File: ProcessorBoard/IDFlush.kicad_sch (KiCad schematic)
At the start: 8 parts, among them U5 74AHCT245, U6 74AHCT16245, U7 74AHCT245, U8 74AHCT16245

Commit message: ProcessorBoard: Update with changes to Control module Ctl_Mid/Ctl_EX issue
This fixes the second issue in Rev D with Ctl_Mid/Ctl_EX.

Two more signals in Hazard Control were using signals from Ctl_Mid when
they should have instead been using signals from Ctl_EX. This fixes an
issue where the control module is unable to correctly detect a RAW hazard
in the EX stage.
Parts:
- U5, U7: value 74AHCT245 -> 74HC245
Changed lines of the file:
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@@
   (paper "A4")
   (title_block
-    (date "2023-11-15")
+    (date "2023-11-19")
     (rev "A")
     (comment 3 "registers must be all ones, which represents a NOP.")
@@
     )
   )
-  (symbol (lib_id "Device:C") (at 33.02 184.15 0) (unit 1)
+  (symbol (lib_id "Device:C") (at 33.02 184.15 0) (mirror y) (unit 1)
     (in_bom yes) (on_board yes) (dnp no)
-    (property "Reference" "C7" (at 35.941 182.9816 0)
+    (property "Reference" "C7" (at 30.099 182.9816 0)
       (effects (font (size 1.27 1.27)) (justify left))
     )
-    (property "Value" "0.1uF" (at 35.941 185.293 0)
+    (property "Value" "0.1uF" (at 30.099 185.293 0)
       (effects (font (size 1.27 1.27)) (justify left))
     )
-    (property "Footprint" "Capacitor_SMD:C_0603_1608Metric_Pad1.08x0.95mm_HandSolder" (at 33.9852 187.96 0)
+    (property "Footprint" "Capacitor_SMD:C_0603_1608Metric_Pad1.08x0.95mm_HandSolder" (at 32.0548 187.96 0)
       (effects (font (size 1.27 1.27)) hide)
     )
@@
       (effects (font (size 1.27 1.27)) (justify left))
     )
-    (property "Value" "74AHCT245" (at 96.8659 114.935 0)
+    (property "Value" "74HC245" (at 96.8659 114.935 0)
       (effects (font (size 1.27 1.27)) (justify left))
     )
@@
       (effects (font (size 1.27 1.27)) (justify left))
     )
-    (property "Value" "74AHCT245" (at 214.2841 114.935 0)
+    (property "Value" "74HC245" (at 214.2841 114.935 0)
       (effects (font (size 1.27 1.27)) (justify left))
     )

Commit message: ProcessorBoard: Use 74ABT where possible over 74AHCT
In several places, the schematics specify 74HC and 74AHCT versions of ICs
where choosing 74ABT would be fine, and would improve performance.
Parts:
- U5, U7: value 74HC245 -> 74ABT245; Mouser (none) -> https://www.mouser.com/ProductDetail/Texas-Instruments/SN74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
- U6, U8: value 74AHCT16245 -> 74ABT16245; Mouser https://www.mouser.com/ProductDetail/Texas-Instruments/74AH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 -> https://www.mouser.com/ProductDetail/Texas-Instruments/74AB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
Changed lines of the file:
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@@
       (effects (font (size 1.27 1.27)) (justify left))
     )
-    (property "Value" "74AHCT16245" (at 110.49 34.925 0)
+    (property "Value" "74ABT16245" (at 110.49 34.925 0)
       (effects (font (size 1.27 1.27)) (justify left))
     )
@@
       (effects (font (size 1.27 1.27)) hide)
     )
-    (property "Datasheet" "" (at 106.68 58.42 0)
-      (effects (font (size 1.27 1.27)) hide)
-    )
-    (property "Mouser" "https://www.mouser.com/ProductDetail/Texas-Instruments/74AHCT16245DLRG4?qs=%2Fha2pyFaduixTLlQ%252B3rIFW8KDPMe6E5CxoQ2Fc519Y9S5BWJ%252B%2FVWeIYQshP1VtN3&utm_source=octopart&utm_medium=aggregator&utm_campaign=595-74AHCT16245DLRG4&utm_content=Texas%20Instruments" (at 101.6 50.8 0)
+    (property "Datasheet" "https://www.ti.com/general/docs/suppproductinfo.tsp?distId=26&gotoUrl=https://www.ti.com/lit/gpn/sn74abt16245a" (at 106.68 58.42 0)
+      (effects (font (size 1.27 1.27)) hide)
+    )
+    (property "Mouser" "https://www.mouser.com/ProductDetail/Texas-Instruments/74ABT16245ADGGRG4?qs=AsTZqt%2FmeqlOzxDYtxnpKQ%3D%3D" (at 101.6 50.8 0)
       (effects (font (size 1.27 1.27)) hide)
     )
@@
       (effects (font (size 1.27 1.27)) (justify left))
     )
-    (property "Value" "74HC245" (at 96.8659 114.935 0)
+    (property "Value" "74ABT245" (at 96.8659 114.935 0)
       (effects (font (size 1.27 1.27)) (justify left))
     )
@@
       (effects (font (size 1.27 1.27)) hide)
     )
-    (property "Datasheet" "http://www.ti.com/lit/gpn/sn74HC245" (at 99.06 132.08 0)
+    (property "Datasheet" "https://www.ti.com/general/docs/suppproductinfo.tsp?distId=26&gotoUrl=https://www.ti.com/lit/gpn/sn74abt245b" (at 99.06 132.08 0)
+      (effects (font (size 1.27 1.27)) hide)
+    )
+    (property "Mouser" "https://www.mouser.com/ProductDetail/Texas-Instruments/SN74ABT245BPWR?qs=5nGYs9Do7G2%2F7Vhs1ZTTgg%3D%3D" (at 99.06 132.08 0)
       (effects (font (size 1.27 1.27)) hide)
     )
@@
       (effects (font (size 1.27 1.27)) (justify left))
     )
-    (property "Value" "74HC245" (at 214.2841 114.935 0)
+    (property "Value" "74ABT245" (at 214.2841 114.935 0)
       (effects (font (size 1.27 1.27)) (justify left))
     )
@@
       (effects (font (size 1.27 1.27)) hide)
     )
-    (property "Datasheet" "http://www.ti.com/lit/gpn/sn74HC245" (at 212.09 132.08 0)
+    (property "Datasheet" "https://www.ti.com/general/docs/suppproductinfo.tsp?distId=26&gotoUrl=https://www.ti.com/lit/gpn/sn74abt245b" (at 212.09 132.08 0)
+      (effects (font (size 1.27 1.27)) hide)
+    )
+    (property "Mouser" "https://www.mouser.com/ProductDetail/Texas-Instruments/SN74ABT245BPWR?qs=5nGYs9Do7G2%2F7Vhs1ZTTgg%3D%3D" (at 212.09 132.08 0)
       (effects (font (size 1.27 1.27)) hide)
     )
@@
       (effects (font (size 1.27 1.27)) (justify left))
     )
-    (property "Value" "74AHCT16245" (at 210.82 34.925 0)
+    (property "Value" "74ABT16245" (at 210.82 34.925 0)
       (effects (font (size 1.27 1.27)) (justify left))
     )
@@
       (effects (font (size 1.27 1.27)) hide)
     )
-    (property "Datasheet" "" (at 214.63 58.42 0)
-      (effects (font (size 1.27 1.27)) hide)
-    )
-    (property "Mouser" "https://www.mouser.com/ProductDetail/Texas-Instruments/74AHCT16245DLRG4?qs=%2Fha2pyFaduixTLlQ%252B3rIFW8KDPMe6E5CxoQ2Fc519Y9S5BWJ%252B%2FVWeIYQshP1VtN3&utm_source=octopart&utm_medium=aggregator&utm_campaign=595-74AHCT16245DLRG4&utm_content=Texas%20Instruments" (at 219.71 50.8 0)
-      (effects (font (size 1.27 1.27)) hide)
-    )
+    (property "Datasheet" "https://www.ti.com/general/docs/suppproductinfo.tsp?distId=26&gotoUrl=https://www.ti.com/lit/gpn/sn74abt16245a" (at 214.63 58.42 0)
+      (effects (font (size 1.27 1.27)) hide)
+    )
+    (property "Mouser" "https://www.mouser.com/ProductDetail/Texas-Instruments/74ABT16245ADGGRG4?qs=AsTZqt%2FmeqlOzxDYtxnpKQ%3D%3D" (at 219.71 50.8 0)
+      (effects (font (size 1.27 1.27)) hide)
+    )

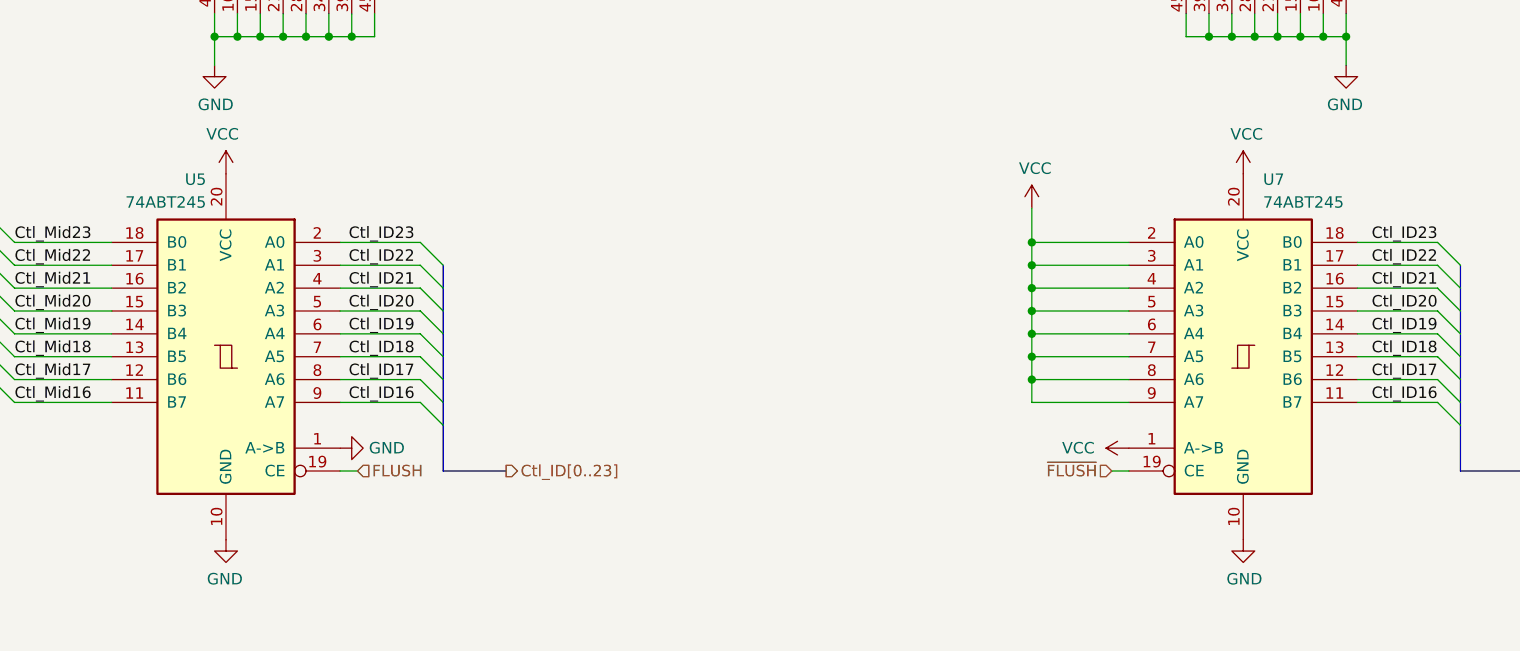
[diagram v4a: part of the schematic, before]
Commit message: ProcessorBoard: Copy symbols into project symbol library, make consistent
Symbols created for Turtle16 have been copied into a project-specific
symbol library. The symbols have all been updated with manufacturer,
manufacturer part number, mouser part number, and digikey part number.

Test points and mounting holes have been marked to be excluded from BOM.
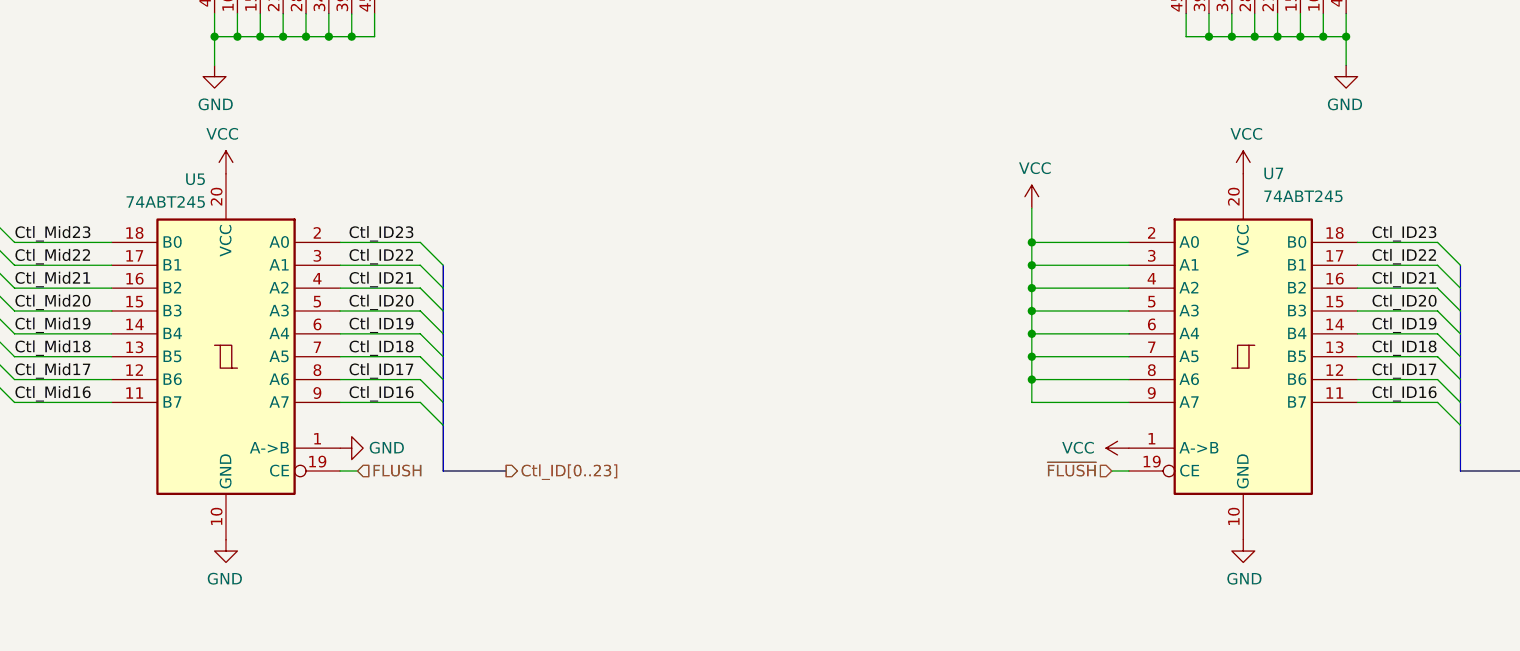
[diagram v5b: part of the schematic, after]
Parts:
- C6, C7, C8, C9: footprint Capacitor_SMD:C_0603_1608Metric_Pad1.08x0.95mm_HandSolder -> Capacitor_SMD:C_0603_1608Metric; Digikey# (none) -> 587-6004-1-ND; Manufacturer (none) -> Taiyo Yuden; Manufacturer# (none) -> EMK107B7104KAHT; Mouser https://www.mouser.com/ProductDetail/963-EMK107B7104KAHT -> (none); Mouser# (none) -> 963-EMK107B7104KAHT
- U5, U7: symbol 74xx:74HC245 -> Turtle16:74ABT245; Digikey# (none) -> 296-3971-1-ND; Manufacturer (none) -> Texas Instruments; Manufacturer# (none) -> SN74ABT245BPWR; Mouser https://www.mouser.com/ProductDetail/Texas-Instruments/SN74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 -> (none); Mouser# (none) -> 595-SN74ABT245BPWR
- U6, U8: symbol 74xx (kicad5):74AHCT16245 -> Turtle16:74ABT16245; Digikey# (none) -> 296-4124-1-ND; Manufacturer (none) -> Texas Instruments; Manufacturer# (none) -> SN74ABTH16245DGGR; Mouser https://www.mouser.com/ProductDetail/Texas-Instruments/74AB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 -> (none); Mouser# (none) -> 595-SNABTH16245DGGR
